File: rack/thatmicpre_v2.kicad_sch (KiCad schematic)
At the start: 89 parts, among them J1 CON-SOCJ-2155, J10 Angled pinheader, J2 NC3FBH2, J3 NC3MBH1, J4 Female header, J5 Male pinheader, J6 Female header, J7 Male pinheader, J8 Angled pinheader, J9 NMJ6HFD2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

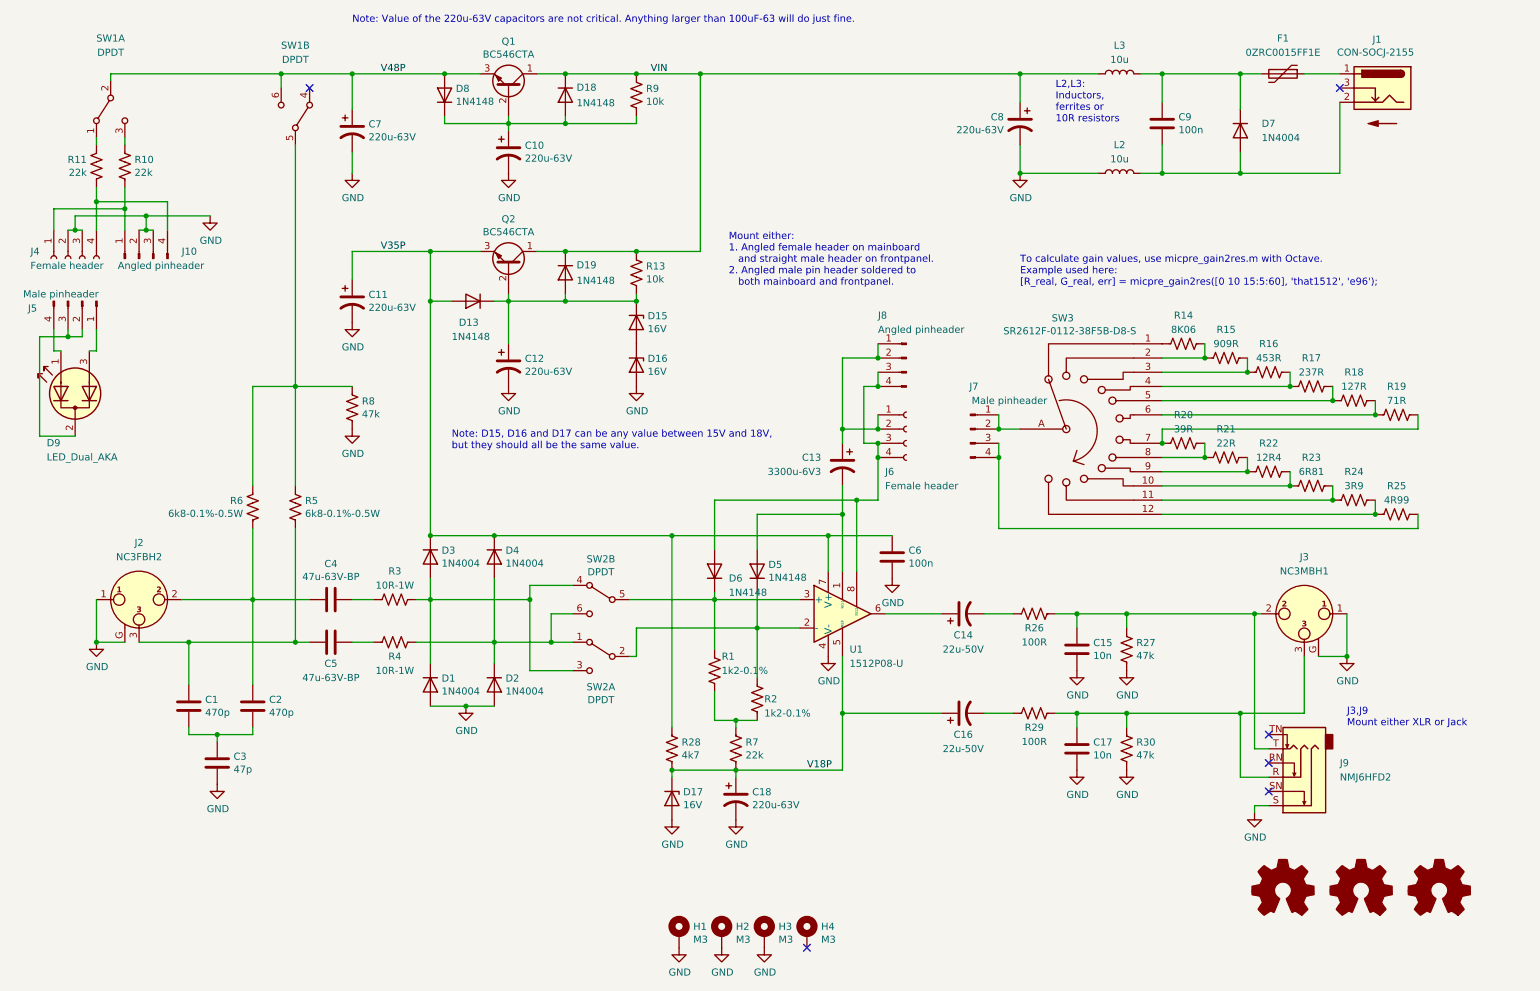
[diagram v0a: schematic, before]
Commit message: change NC3MBH1 to be NCJ6FA-H
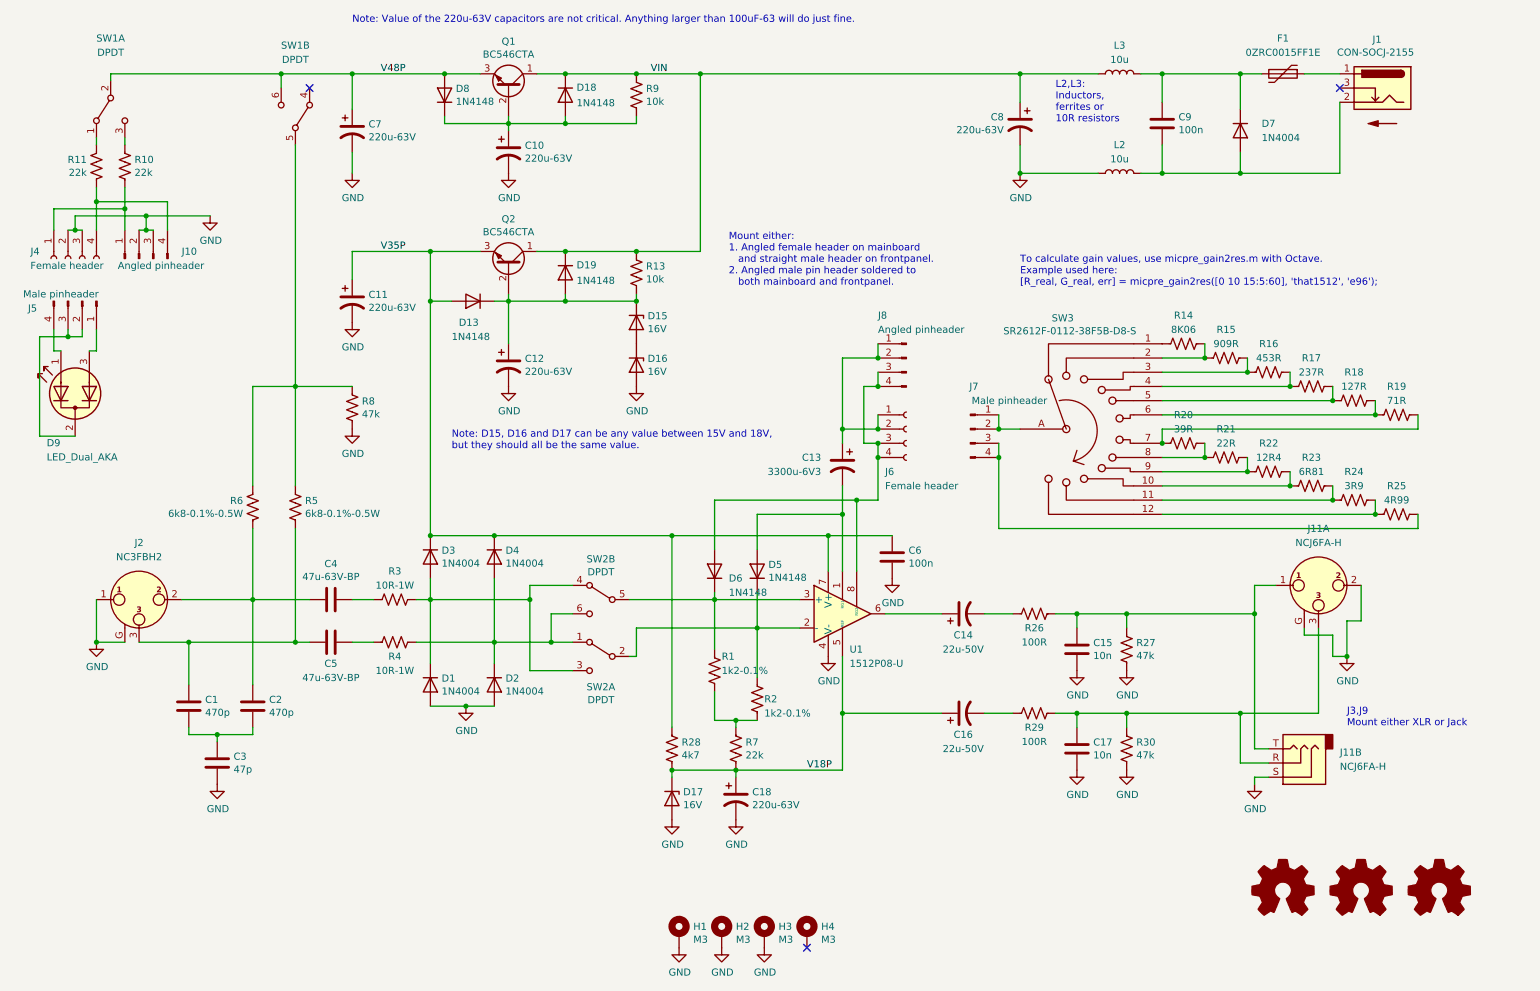
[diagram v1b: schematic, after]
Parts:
- removed J3: NC3MBH1, Connector_Audio:Jack_XLR_Neutrik_NC3MBH_Horizontal, symbol Connector:XLR3_Ground
- removed J9: NMJ6HFD2, Connector_Audio:Jack_6.35mm_Neutrik_NMJ6HFD2_Horizontal, symbol Connector:AudioJack3_Switch
- added J11: NCJ6FA-H, Connector_Audio:Jack_XLR-6.35mm_Neutrik_NCJ6FA-H_Horizontal, symbol Connector_Audio:NCJ6FA-H
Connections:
- net GND: now also J11.2, J11.G, J11.S
- net at C15.1, R26.1, R27.1: now also J11.1, J11.T
- net at C17.1, R29.1, R30.1: now also J11.3, J11.R
- no-connect marks 6 -> 3

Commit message: Fixed bug, NCJ6FA-H where 1-2pin connections were interchanged
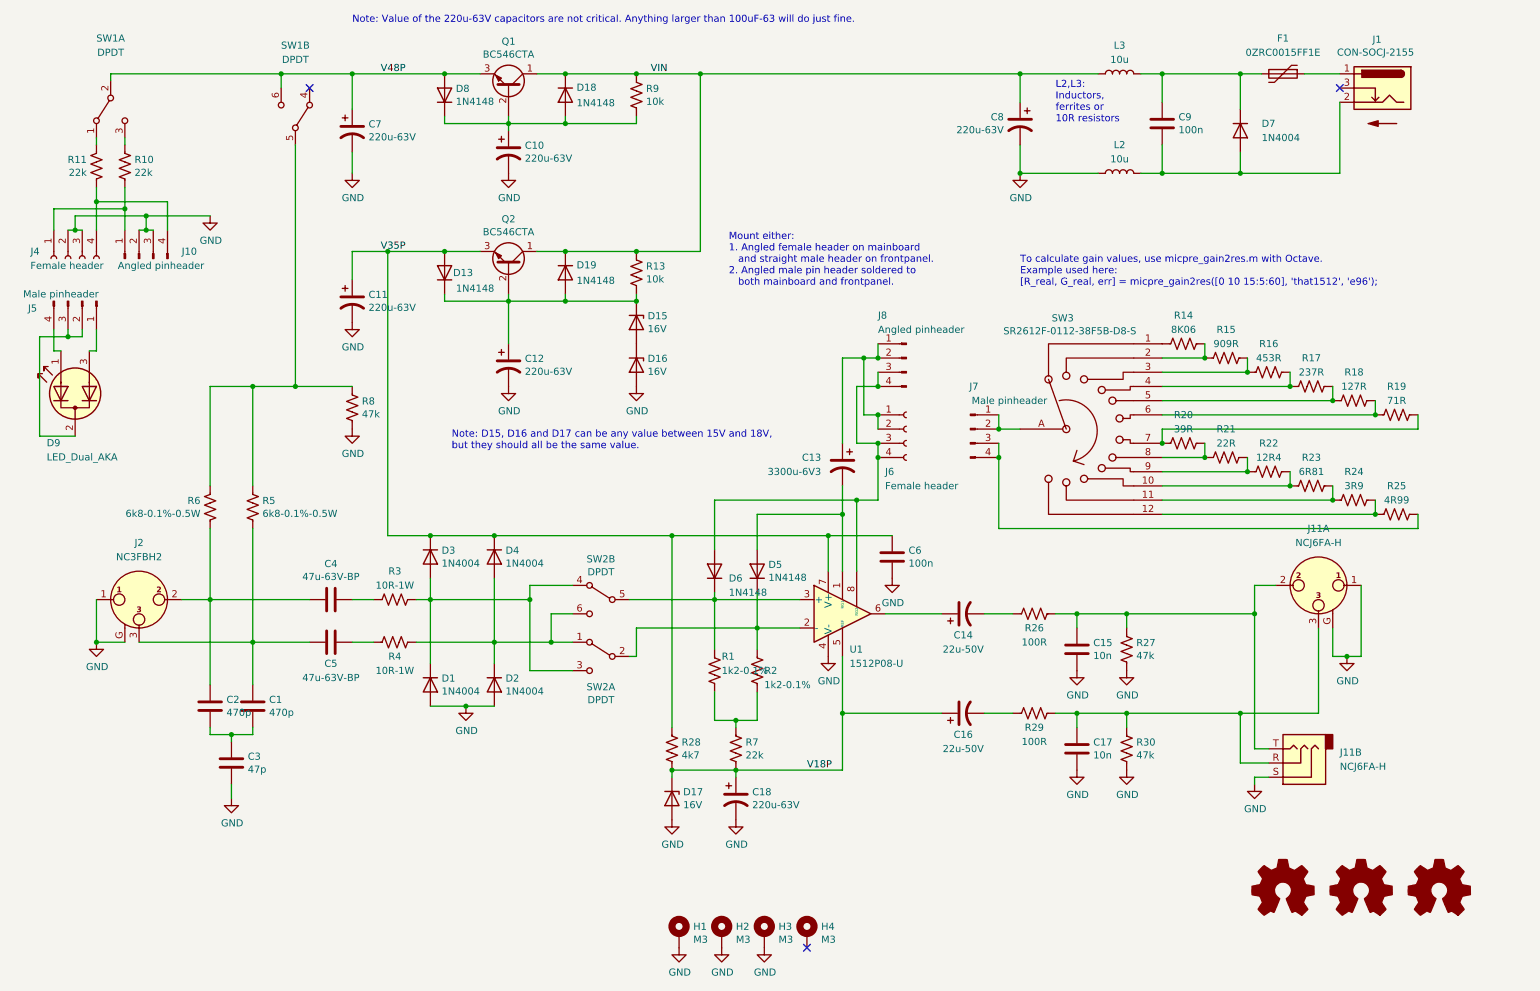
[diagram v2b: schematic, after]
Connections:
- net GND: now also J11.1; no longer J11.2
- net at C15.1, J11.T, R26.1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: now also J11.2; no longer J11.1
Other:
- note removed: "J3,J9 Mount either XLR or Jack"
- moved on the sheet: C1, C2, C3, D13, R2, R5, R6

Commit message: Modify the footprints of 0.5W and 1W resistors
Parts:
- R3, R4: footprint Resistor_THT:R_Axial_DIN0207_L6.3mm_D2.5mm_P10.16mm_Horizontal -> Resistor_THT:R_Axial_DIN0411_L9.9mm_D3.6mm_P15.24mm_Horizontal
- R5, R6: footprint Resistor_THT:R_Axial_DIN0207_L6.3mm_D2.5mm_P10.16mm_Horizontal -> Resistor_THT:R_Axial_DIN0309_L9.0mm_D3.2mm_P12.70mm_Horizontal
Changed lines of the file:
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@@
 			)
 		)
-		(property "Footprint" "Resistor_THT:R_Axial_DIN0207_L6.3mm_D2.5mm_P10.16mm_Horizontal"
+		(property "Footprint" "Resistor_THT:R_Axial_DIN0309_L9.0mm_D3.2mm_P12.70mm_Horizontal"
 			(at 53.594 105.664 90)
 			(effects
@@
 			)
 		)
-		(property "Footprint" "Resistor_THT:R_Axial_DIN0207_L6.3mm_D2.5mm_P10.16mm_Horizontal"
+		(property "Footprint" "Resistor_THT:R_Axial_DIN0309_L9.0mm_D3.2mm_P12.70mm_Horizontal"
 			(at 63.246 105.664 90)
 			(effects
@@
 			)
 		)
-		(property "Footprint" "Resistor_THT:R_Axial_DIN0207_L6.3mm_D2.5mm_P10.16mm_Horizontal"
+		(property "Footprint" "Resistor_THT:R_Axial_DIN0411_L9.9mm_D3.6mm_P15.24mm_Horizontal"
 			(at 87.376 130.556 90)
 			(effects
@@
 			)
 		)
-		(property "Footprint" "Resistor_THT:R_Axial_DIN0207_L6.3mm_D2.5mm_P10.16mm_Horizontal"
+		(property "Footprint" "Resistor_THT:R_Axial_DIN0411_L9.9mm_D3.6mm_P15.24mm_Horizontal"
 			(at 87.376 122.936 90)
 			(effects
